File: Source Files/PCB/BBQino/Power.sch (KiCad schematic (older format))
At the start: 9 parts, among them Q1 IPD068P03L3G

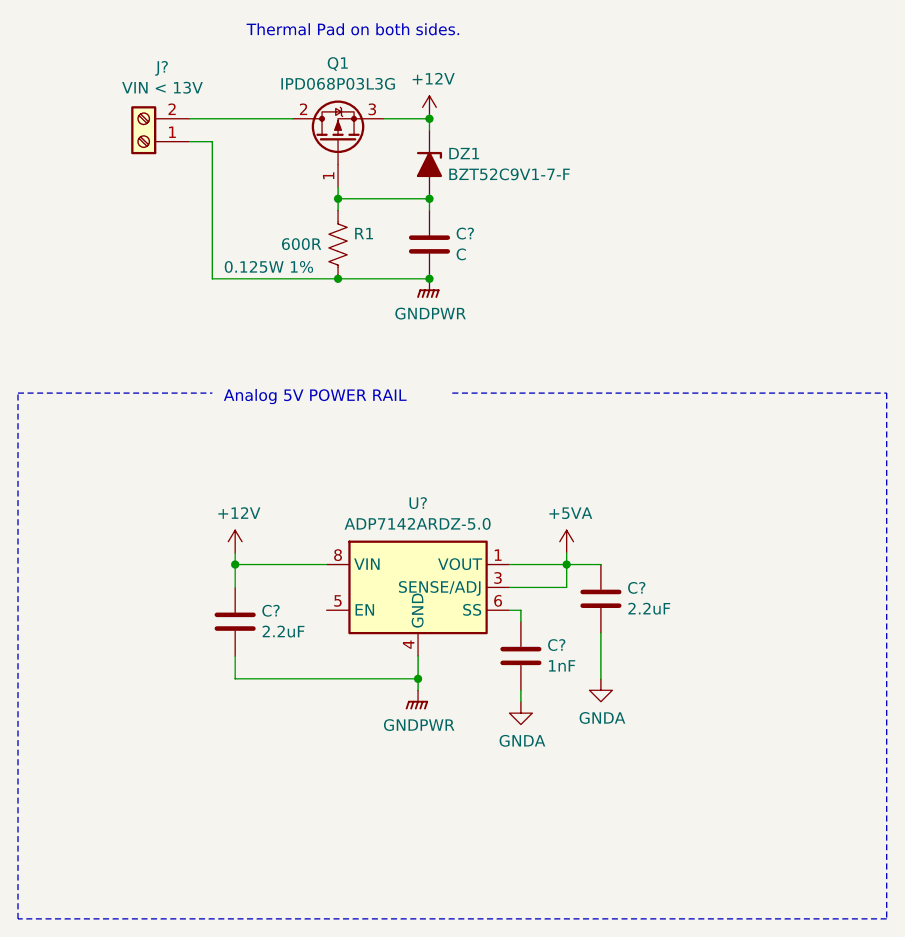
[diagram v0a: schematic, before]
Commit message: 230V section first Draft. Added external module on top of the shield for the 230V section
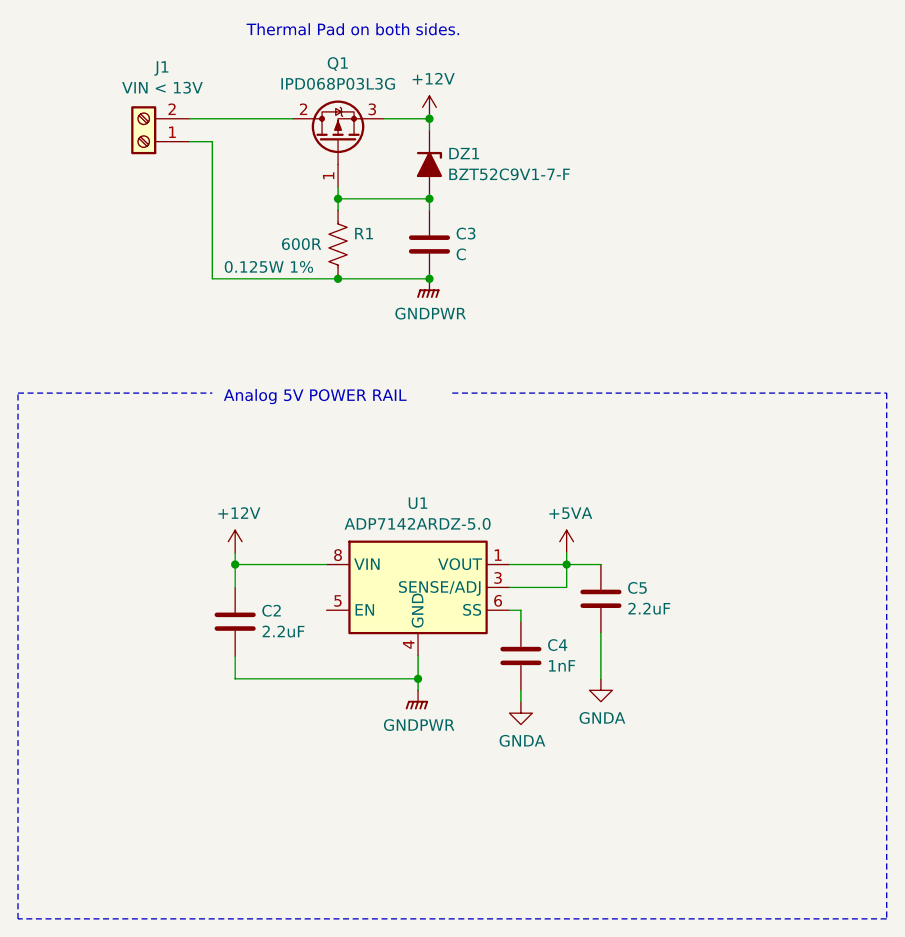
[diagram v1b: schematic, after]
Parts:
- gave numbers to parts that had none: 6
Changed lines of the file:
@@
 $EndDescr
 $Comp
-L BBQino-rescue:Screw_Terminal_01x02-Connector J?
+L BBQino-rescue:Screw_Terminal_01x02-Connector J1
 U 1 1 6143D9E7
 P 1250 1250
-F 0 "J?" H 1168 925 50  0000 C CNN
+F 0 "J1" H 1168 925 50  0000 C CNN
 F 1 "VIN < 13V" H 1168 1016 50  0000 C CNN
 F 2 "TerminalBlock_TE-Connectivity:TerminalBlock_TE_282834-2_1x02_P2.54mm_Horizontal" H 1250 1250 50  0001 C CNN
@@
 $EndComp
 $Comp
-L BBQino-rescue:C-Device C?
+L BBQino-rescue:C-Device C3
 U 1 1 61442C4C
 P 2500 1700
-F 0 "C?" H 2615 1746 50  0000 L CNN
+F 0 "C3" H 2615 1746 50  0000 L CNN
 F 1 "C" H 2615 1655 50  0000 L CNN
 F 2 "" H 2538 1550 50  0001 C CNN
@@
 	1450 1150 1900 1150
 $Comp
-L BBQino-rescue:+12V-power #PWR?
+L BBQino-rescue:+12V-power #PWR0106
 U 1 1 6144570A
 P 2500 1150
-F 0 "#PWR?" H 2500 1000 50  0001 C CNN
+F 0 "#PWR0106" H 2500 1000 50  0001 C CNN
 F 1 "+12V" H 2515 1323 50  0000 C CNN
 F 2 "" H 2500 1150 50  0001 C CNN
@@
 Connection ~ 2500 1150
 $Comp
-L BBQino-rescue:GNDPWR-power #PWR?
+L BBQino-rescue:GNDPWR-power #PWR0107
 U 1 1 61445C4C
 P 2500 1850
-F 0 "#PWR?" H 2500 1650 50  0001 C CNN
+F 0 "#PWR0107" H 2500 1650 50  0001 C CNN
 F 1 "GNDPWR" H 2504 1696 50  0000 C CNN
 F 2 "" H 2500 1800 50  0001 C CNN
@@
 Analog 5V POWER RAIL\n
 $Comp
-L BBQino-rescue:C-Device C?
+L BBQino-rescue:C-Device C5
 U 1 1 6144ECB3
 P 3250 3250
-F 0 "C?" H 3365 3296 50  0000 L CNN
+F 0 "C5" H 3365 3296 50  0000 L CNN
 F 1 "2.2uF" H 3365 3205 50  0000 L CNN
 F 2 "" H 3288 3100 50  0001 C CNN
@@
 $EndComp
 $Comp
-L BBQino-rescue:C-Device C?
+L BBQino-rescue:C-Device C2
 U 1 1 6144F727
 P 1650 3350
-F 0 "C?" H 1765 3396 50  0000 L CNN
+F 0 "C2" H 1765 3396 50  0000 L CNN
 F 1 "2.2uF" H 1765 3305 50  0000 L CNN
 F 2 "" H 1688 3200 50  0001 C CNN
@@
 $EndComp
 $Comp
-L BBQino-rescue:+12V-power #PWR?
+L BBQino-rescue:+12V-power #PWR0108
 U 1 1 614537EF
 P 1650 3050
-F 0 "#PWR?" H 1650 2900 50  0001 C CNN
+F 0 "#PWR0108" H 1650 2900 50  0001 C CNN
 F 1 "+12V" H 1665 3223 50  0000 C CNN
 F 2 "" H 1650 3050 50  0001 C CNN
@@
 	3100 3100 2850 3100
 $Comp
-L BBQino-rescue:+5VA-power #PWR?
+L BBQino-rescue:+5VA-power #PWR0109
 U 1 1 61456D2F
 P 3100 3050
-F 0 "#PWR?" H 3100 2900 50  0001 C CNN
+F 0 "#PWR0109" H 3100 2900 50  0001 C CNN
 F 1 "+5VA" H 3115 3223 50  0000 C CNN
 F 2 "" H 3100 3050 50  0001 C CNN
@@
 $EndComp
 $Comp
-L BBQino-rescue:GNDA-power #PWR?
+L BBQino-rescue:GNDA-power #PWR0110
 U 1 1 61457278
 P 3250 3600
-F 0 "#PWR?" H 3250 3350 50  0001 C CNN
+F 0 "#PWR0110" H 3250 3350 50  0001 C CNN
 F 1 "GNDA" H 3255 3427 50  0000 C CNN
 F 2 "" H 3250 3600 50  0001 C CNN
@@
 $EndComp
 $Comp
-L BBQino-rescue:GNDPWR-power #PWR?
+L BBQino-rescue:GNDPWR-power #PWR0111
 U 1 1 61459FC8
 P 2450 3650
-F 0 "#PWR?" H 2450 3450 50  0001 C CNN
+F 0 "#PWR0111" H 2450 3450 50  0001 C CNN
 F 1 "GNDPWR" H 2454 3496 50  0000 C CNN
 F 2 "" H 2450 3600 50  0001 C CNN
@@
 	3100 3100 3100 3050
 $Comp
-L BBQino-rescue:ADP7142ARDZ-5.0-Regulator_Linear U?
+L BBQino-rescue:ADP7142ARDZ-5.0-Regulator_Linear U1
 U 1 1 614681CA
 P 2450 3200
-F 0 "U?" H 2450 3567 50  0000 C CNN
+F 0 "U1" H 2450 3567 50  0000 C CNN
 F 1 "ADP7142ARDZ-5.0" H 2450 3476 50  0000 C CNN
 F 2 "Package_SO:SOIC-8-1EP_3.9x4.9mm_P1.27mm_EP2.29x3mm" H 2450 2800 50  0001 C CIN
@@
 	3100 3100 3250 3100
 $Comp
-L BBQino-rescue:C-Device C?
+L BBQino-rescue:C-Device C4
 U 1 1 61474DD5
 P 2900 3500
-F 0 "C?" H 3015 3546 50  0000 L CNN
+F 0 "C4" H 3015 3546 50  0000 L CNN
 F 1 "1nF" H 3015 3455 50  0000 L CNN
 F 2 "" H 2938 3350 50  0001 C CNN
@@
 	2900 3700 2900 3650
 $Comp
-L BBQino-rescue:GNDA-power #PWR?
+L BBQino-rescue:GNDA-power #PWR0112
 U 1 1 61476818
 P 2900 3700
-F 0 "#PWR?" H 2900 3450 50  0001 C CNN
+F 0 "#PWR0112" H 2900 3450 50  0001 C CNN
 F 1 "GNDA" H 2905 3527 50  0000 C CNN
 F 2 "" H 2900 3700 50  0001 C CNN
